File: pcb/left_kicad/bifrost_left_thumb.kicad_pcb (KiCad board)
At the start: 2 copper layers, 58.5 x 21 mm, 12 parts, among them J1 Conn_01x06, SW1 1U, SW2 1U, SW3 1U

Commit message: Update PCB and case designs
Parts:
- moved C3 56.1 mm to (118.1, 65.7)
- moved H2 56.1 mm to (109.0, 59.8)
- moved C1 56.1 mm to (80.3, 65.7)
- moved C2 56.1 mm to (99.2, 64.7)
- moved D1 56.1 mm to (81.0, 65.6)
- moved D3 56.1 mm to (118.8, 65.8)
- moved SW2 56.1 mm to (99.2, 59.5)
- moved D2 56.1 mm to (99.9, 64.7)
- moved H1 56.1 mm to (89.5, 59.8)
- moved J1 56.1 mm to (96.0, 50.4)
- moved SW1 56.1 mm to (79.8, 60.6)
- moved SW3 56.1 mm to (118.7, 60.6)
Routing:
- net GND: vias 0 -> 86

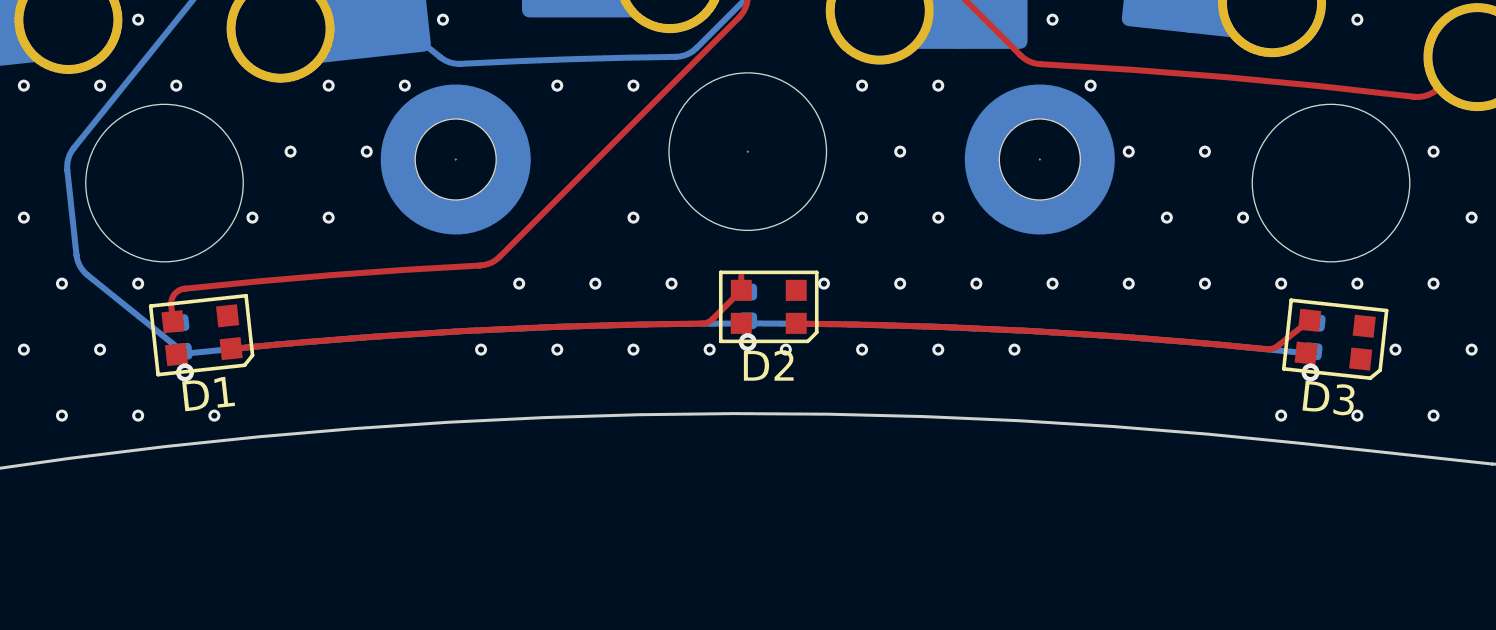
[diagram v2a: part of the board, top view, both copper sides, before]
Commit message: Update PCB fabrication outputs and switch knob
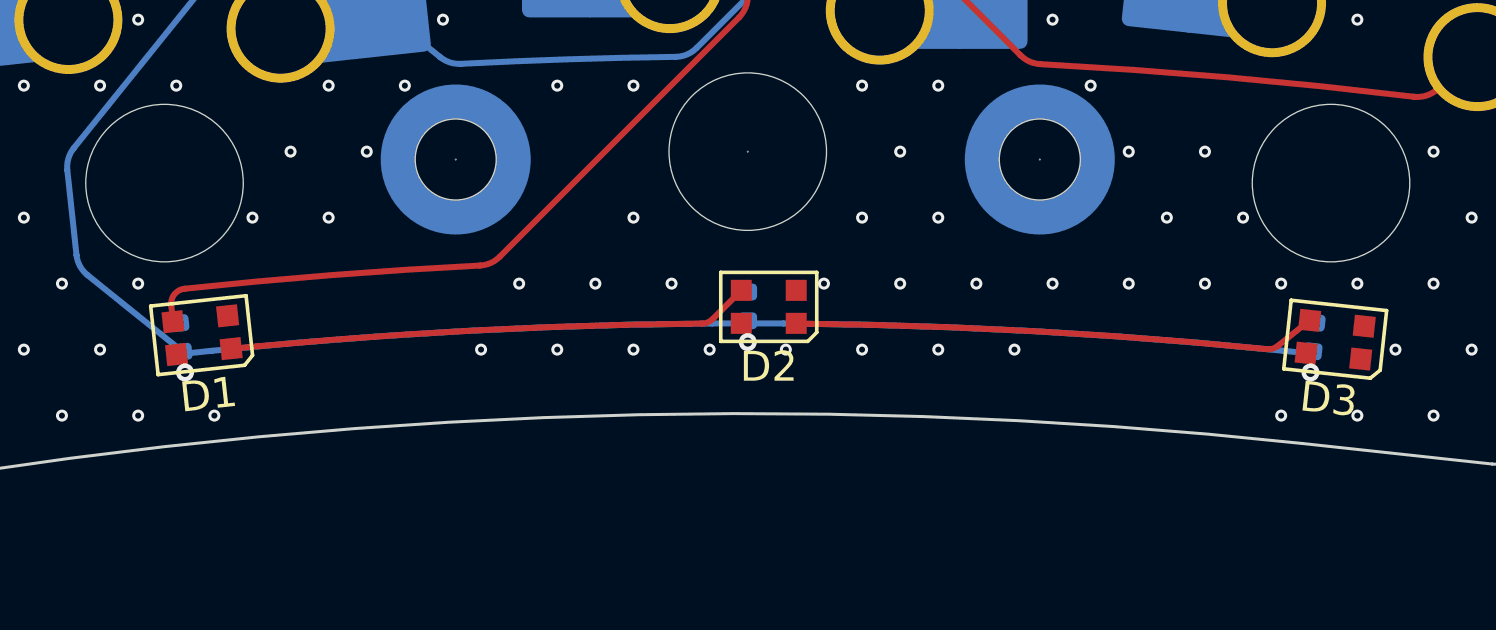
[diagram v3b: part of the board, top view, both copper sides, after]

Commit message: Update PCB designs and fabrication outputs
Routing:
- net RGB_PWR: track 73.7 -> 74.9 mm

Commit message: Update PCB layouts and production files
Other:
- board text added: "Bifrost rev.1.0"

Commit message: Update Bifrost case and PCB outputs
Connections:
- J1 pad 2: RGB -> GND
- J1 pad 3: GND -> RGB
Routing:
- net RGB: track 28.8 -> 28.2 mm

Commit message: Update PCB mounting hardware footprints
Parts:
- H1, H2: footprint Smidr:MountingHole_TH-1.6-M2 -> Smidr:SMD-1_BD4.4-D2.8
- turned H1 to 0 degrees
- turned H2 to 0 degrees
